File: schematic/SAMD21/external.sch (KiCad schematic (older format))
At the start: 19 parts, among them IC3 MCP2221-I_SL, J10 Conn_02x06_Odd_Even, J11 Conn_02x06_Odd_Even, J12 Conn_02x06_Odd_Even, J13 Conn_01x02, J14 Conn_02x05_Odd_Even, J15 Conn_01x08, J8 Conn_02x02_Odd_Even, J9 Conn_02x02_Odd_Even

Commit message: Complete schematic
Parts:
- J10: footprint (none) -> Connector_PinHeader_2.54mm:PinHeader_2x06_P2.54mm_Vertical
- J12: footprint (none) -> Connector_PinHeader_2.54mm:PinHeader_2x06_P2.54mm_Vertical_SMD
- J14: footprint (none) -> Connector_PinHeader_2.54mm:PinHeader_2x05_P2.54mm_Vertical
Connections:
- net labels added: D+, D-, PA02, PA03, PA04, PA05, PA06, PA07, PA08, PA09, PA10, PA11, PA12, PA13, PA14, PA15, PA16, PA17, PA18, PA19, PA20, PA21, PA22, PA23, PA27, PA28, PB08, PB09, PB10, PB11, PB22, PB23
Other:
- moved on the sheet: J11, J12, J14
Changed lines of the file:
@@
 L Connector_Generic:Conn_02x06_Odd_Even J11
 U 1 1 61799C22
-P 4850 5800
-F 0 "J11" H 4900 6125 50  0000 C CNN
-F 1 "Conn_02x06_Odd_Even" H 4900 6126 50  0001 C CNN
-F 2 "Connector_PinHeader_2.54mm:PinHeader_2x06_P2.54mm_Vertical" H 4850 5800 50  0001 C CNN
-F 3 "~" H 4850 5800 50  0001 C CNN
-	1    4850 5800
-	1    0    0    -1
-$EndComp
-Text GLabel 7200 4350 0    50   Input ~ 0
-VCC3V3
-Text GLabel 4550 5600 0    50   Input ~ 0
-VCC3V3
-Text GLabel 7500 5650 0    50   Input ~ 0
+P 4800 5800
+F 0 "J11" H 4850 6125 50  0000 C CNN
+F 1 "Conn_02x06_Odd_Even" H 4850 6126 50  0001 C CNN
+F 2 "Connector_PinHeader_2.54mm:PinHeader_2x06_P2.54mm_Vertical" H 4800 5800 50  0001 C CNN
+F 3 "~" H 4800 5800 50  0001 C CNN
+	1    4800 5800
+	1    0    0    -1
+$EndComp
+Text GLabel 7200 4300 0    50   Input ~ 0
+VCC3V3
+Text GLabel 4500 5600 0    50   Input ~ 0
+VCC3V3
+Text GLabel 7200 5600 0    50   Input ~ 0
 VCC3V3
 $Comp
 L power:GND #PWR029
 U 1 1 617AC5C9
-P 7800 4350
-F 0 "#PWR029" H 7800 4100 50  0001 C CNN
-F 1 "GND" V 7805 4222 50  0000 R CNN
-F 2 "" H 7800 4350 50  0001 C CNN
-F 3 "" H 7800 4350 50  0001 C CNN
-	1    7800 4350
+P 7800 4300
+F 0 "#PWR029" H 7800 4050 50  0001 C CNN
+F 1 "GND" V 7805 4172 50  0000 R CNN
+F 2 "" H 7800 4300 50  0001 C CNN
+F 3 "" H 7800 4300 50  0001 C CNN
+	1    7800 4300
 	0    -1   -1   0
 $EndComp
@@
 L power:GND #PWR027
 U 1 1 617B03D0
-P 5150 5600
-F 0 "#PWR027" H 5150 5350 50  0001 C CNN
-F 1 "GND" V 5155 5472 50  0000 R CNN
-F 2 "" H 5150 5600 50  0001 C CNN
-F 3 "" H 5150 5600 50  0001 C CNN
-	1    5150 5600
+P 5100 5600
+F 0 "#PWR027" H 5100 5350 50  0001 C CNN
+F 1 "GND" V 5105 5472 50  0000 R CNN
+F 2 "" H 5100 5600 50  0001 C CNN
+F 3 "" H 5100 5600 50  0001 C CNN
+	1    5100 5600
 	0    -1   -1   0
 $EndComp
@@
 L power:GND #PWR030
 U 1 1 617B4203
-P 8100 5650
-F 0 "#PWR030" H 8100 5400 50  0001 C CNN
-F 1 "GND" V 8105 5522 50  0000 R CNN
-F 2 "" H 8100 5650 50  0001 C CNN
-F 3 "" H 8100 5650 50  0001 C CNN
-	1    8100 5650
+P 7800 5600
+F 0 "#PWR030" H 7800 5350 50  0001 C CNN
+F 1 "GND" V 7805 5472 50  0000 R CNN
+F 2 "" H 7800 5600 50  0001 C CNN
+F 3 "" H 7800 5600 50  0001 C CNN
+	1    7800 5600
 	0    -1   -1   0
 $EndComp
@@
 	5200 4400 5100 4400
 Wire Wire Line
-	7200 4350 7300 4350
-Wire Wire Line
-	7300 4450 7200 4450
-Wire Wire Line
-	7200 4550 7300 4550
-Wire Wire Line
-	7300 4650 7200 4650
-Wire Wire Line
-	7200 4750 7300 4750
-Wire Wire Line
-	7300 4850 7200 4850
-Wire Wire Line
-	7900 4850 7800 4850
-Wire Wire Line
-	7800 4750 7900 4750
-Wire Wire Line
-	7900 4650 7800 4650
-Wire Wire Line
-	7800 4550 7900 4550
-Wire Wire Line
-	7900 4450 7800 4450
-Wire Wire Line
-	4550 5600 4650 5600
-Wire Wire Line
-	4650 5700 4550 5700
-Wire Wire Line
-	4550 5800 4650 5800
-Wire Wire Line
-	4650 5900 4550 5900
-Wire Wire Line
-	4550 6000 4650 6000
-Wire Wire Line
-	4550 6100 4650 6100
-Wire Wire Line
-	5150 6100 5250 6100
-Wire Wire Line
-	5250 6000 5150 6000
-Wire Wire Line
-	5150 5900 5250 5900
-Wire Wire Line
-	5250 5800 5150 5800
-Wire Wire Line
-	5150 5700 5250 5700
-Wire Wire Line
-	7600 5650 7500 5650
-Wire Wire Line
-	7500 5750 7600 5750
-Wire Wire Line
-	8100 5850 8200 5850
-Wire Wire Line
-	8200 5950 8100 5950
-Wire Wire Line
-	8100 6050 8200 6050
-Wire Wire Line
-	7600 6050 7500 6050
-Wire Wire Line
-	7500 5950 7600 5950
-Wire Wire Line
-	8100 5750 8200 5750
+	7200 4300 7300 4300
+Wire Wire Line
+	7300 4400 7200 4400
+Wire Wire Line
+	7200 4500 7300 4500
+Wire Wire Line
+	7300 4600 7200 4600
+Wire Wire Line
+	7200 4700 7300 4700
+Wire Wire Line
+	7300 4800 7200 4800
+Wire Wire Line
+	7900 4800 7800 4800
+Wire Wire Line
+	7800 4700 7900 4700
+Wire Wire Line
+	7900 4600 7800 4600
+Wire Wire Line
+	7800 4500 7900 4500
+Wire Wire Line
+	7900 4400 7800 4400
+Wire Wire Line
+	4500 5600 4600 5600
+Wire Wire Line
+	4600 5700 4500 5700
+Wire Wire Line
+	4500 5800 4600 5800
+Wire Wire Line
+	4600 5900 4500 5900
+Wire Wire Line
+	4500 6000 4600 6000
+Wire Wire Line
+	4500 6100 4600 6100
+Wire Wire Line
+	5100 6100 5200 6100
+Wire Wire Line
+	5200 6000 5100 6000
+Wire Wire Line
+	5100 5900 5200 5900
+Wire Wire Line
+	5200 5800 5100 5800
+Wire Wire Line
+	5100 5700 5200 5700
+Wire Wire Line
+	7300 5600 7200 5600
+Wire Wire Line
+	7200 5700 7300 5700
+Wire Wire Line
+	7800 5800 7900 5800
+Wire Wire Line
+	7900 5900 7800 5900
+Wire Wire Line
+	7800 6000 7900 6000
+Wire Wire Line
+	7300 6000 7200 6000
+Wire Wire Line
+	7200 5900 7300 5900
+Wire Wire Line
+	7800 5700 7900 5700
 $Comp
 L Connector_Generic:Conn_01x08 J15
@@
 Program/Debug
 Wire Wire Line
-	7500 5850 7600 5850
+	7200 5800 7300 5800
 Text Notes 2900 2900 0    50   ~ 0
 SERCOM1
@@
 F 0 "J10" H 4850 4825 50  0000 C CNN
 F 1 "Conn_02x06_Odd_Even" H 4850 4826 50  0001 C CNN
-F 2 "" H 4800 4500 50  0001 C CNN
+F 2 "Connector_PinHeader_2.54mm:PinHeader_2x06_P2.54mm_Vertical" H 4800 4500 50  0001 C CNN
 F 3 "~" H 4800 4500 50  0001 C CNN
 	1    4800 4500
@@
 L Connector_Generic:Conn_02x06_Odd_Even J12
 U 1 1 619CB274
-P 7500 4550
-F 0 "J12" H 7550 4875 50  0000 C CNN
-F 1 "Conn_02x06_Odd_Even" H 7550 4876 50  0001 C CNN
-F 2 "" H 7500 4550 50  0001 C CNN
-F 3 "~" H 7500 4550 50  0001 C CNN
-	1    7500 4550
+P 7500 4500
+F 0 "J12" H 7550 4825 50  0000 C CNN
+F 1 "Conn_02x06_Odd_Even" H 7550 4826 50  0001 C CNN
+F 2 "Connector_PinHeader_2.54mm:PinHeader_2x06_P2.54mm_Vertical_SMD" H 7500 4500 50  0001 C CNN
+F 3 "~" H 7500 4500 50  0001 C CNN
+	1    7500 4500
 	1    0    0    -1
 $EndComp
@@
 L Connector_Generic:Conn_02x05_Odd_Even J14
 U 1 1 619D2D7D
-P 7800 5850
-F 0 "J14" H 7850 6175 50  0000 C CNN
-F 1 "Conn_02x05_Odd_Even" H 7850 6176 50  0001 C CNN
-F 2 "" H 7800 5850 50  0001 C CNN
-F 3 "~" H 7800 5850 50  0001 C CNN
-	1    7800 5850
-	1    0    0    -1
-$EndComp
+P 7500 5800
+F 0 "J14" H 7550 6125 50  0000 C CNN
+F 1 "Conn_02x05_Odd_Even" H 7550 6126 50  0001 C CNN
+F 2 "Connector_PinHeader_2.54mm:PinHeader_2x05_P2.54mm_Vertical" H 7500 5800 50  0001 C CNN
+F 3 "~" H 7500 5800 50  0001 C CNN
+	1    7500 5800
+	1    0    0    -1
+$EndComp
+Text GLabel 4500 4400 0    50   Input ~ 0
+SERCOM1_PAD0
+Text GLabel 5200 4400 2    50   Input ~ 0
+SERCOM1_PAD1
+Text GLabel 4500 4500 0    50   Input ~ 0
+PA02
+Text GLabel 5200 4500 2    50   Input ~ 0
+PA03
+Text GLabel 4500 4600 0    50   Input ~ 0
+PB08
+Text GLabel 5200 4600 2    50   Input ~ 0
+PB09
+Text GLabel 4500 4700 0    50   Input ~ 0
+PA04
+Text GLabel 5200 4700 2    50   Input ~ 0
+PA05
+Text GLabel 4500 4800 0    50   Input ~ 0
+PA06
+Text GLabel 5200 4800 2    50   Input ~ 0
+PA07
+Text GLabel 4500 5700 0    50   Input ~ 0
+PA08
+Text GLabel 5200 5700 2    50   Input ~ 0
+PA09
+Text GLabel 4500 5800 0    50   Input ~ 0
+PA10
+Text GLabel 5200 5800 2    50   Input ~ 0
+PA11
+Text GLabel 4500 5900 0    50   Input ~ 0
+PB10
+Text GLabel 5200 5900 2    50   Input ~ 0
+PB11
+Text GLabel 4500 6000 0    50   Input ~ 0
+PA12
+Text GLabel 5200 6000 2    50   Input ~ 0
+PA13
+Text GLabel 4500 6100 0    50   Input ~ 0
+PA14
+Text GLabel 5200 6100 2    50   Input ~ 0
+PA15
+Text GLabel 7200 4400 0    50   Input ~ 0
+PA16
+Text GLabel 7900 4400 2    50   Input ~ 0
+PA17
+Text GLabel 7200 4500 0    50   Input ~ 0
+PA18
+Text GLabel 7900 4500 2    50   Input ~ 0
+PA19
+Text GLabel 7200 4600 0    50   Input ~ 0
+PA20
+Text GLabel 7900 4600 2    50   Input ~ 0
+PA21
+Text GLabel 7200 4700 0    50   Input ~ 0
+PA22
+Text GLabel 7900 4700 2    50   Input ~ 0
+PA23
+Text GLabel 7200 4800 0    50   Input ~ 0
+D-
+Text GLabel 7900 4800 2    50   Input ~ 0
+D+
+Text GLabel 7200 5700 0    50   Input ~ 0
+PB22
+Text GLabel 7900 5700 2    50   Input ~ 0
+PB23
+Text GLabel 7200 5800 0    50   Input ~ 0
+PA27
+Text GLabel 7900 5800 2    50   Input ~ 0
+PA28
+Text GLabel 7200 5900 0    50   Input ~ 0
+SWCLK
+Text GLabel 7900 5900 2    50   Input ~ 0
+SWDIO
+Text GLabel 7200 6000 0    50   Input ~ 0
+SERCOM5_PAD0
+Text GLabel 7900 6000 2    50   Input ~ 0
+SERCOM5_PAD1
 $EndSCHEMATC

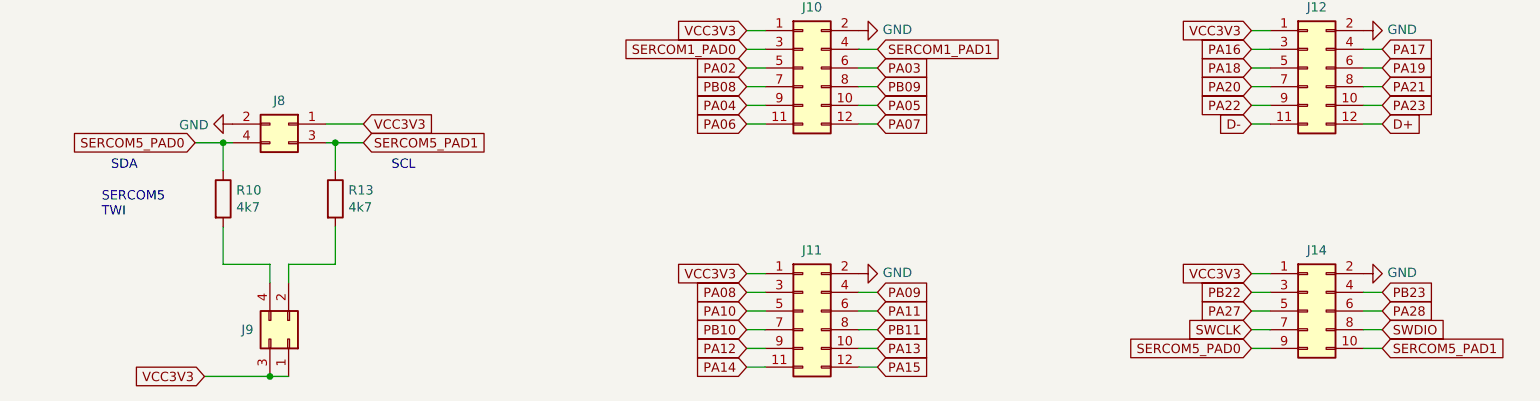
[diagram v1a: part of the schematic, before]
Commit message: Moved I2C to pins with support for I2C
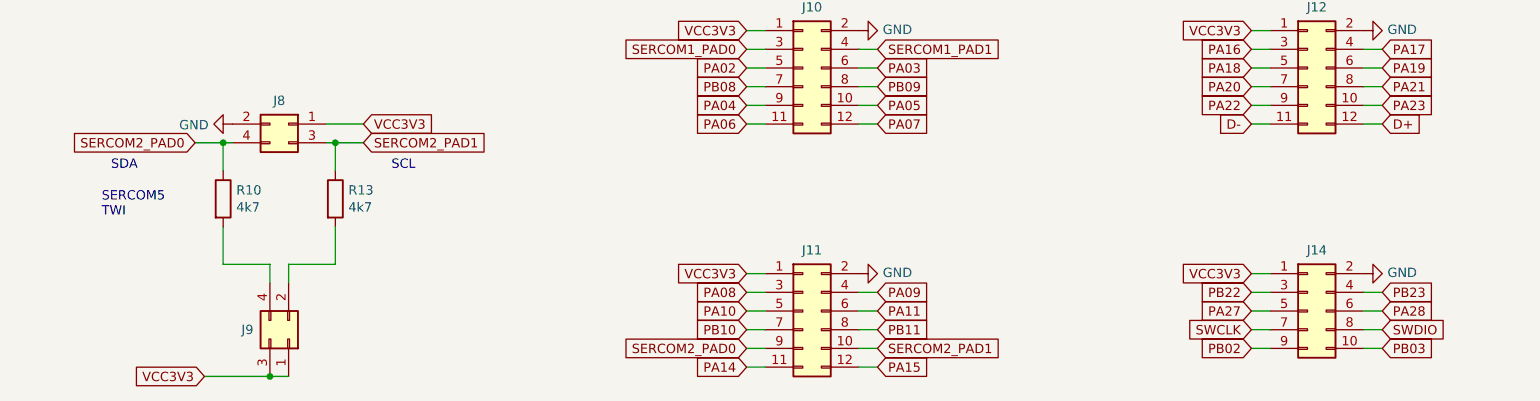
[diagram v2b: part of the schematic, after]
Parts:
- J12: footprint Connector_PinHeader_2.54mm:PinHeader_2x06_P2.54mm_Vertical_SMD -> Connector_PinHeader_2.54mm:PinHeader_2x06_P2.54mm_Vertical
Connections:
- net PA12 renamed SERCOM2_PAD0
- net SERCOM2_PAD0: now also J8.4 (Pin_4), R10.1
- net PA13 renamed SERCOM2_PAD1
- net SERCOM2_PAD1: now also J8.3 (Pin_3), R13.1
- removed net SERCOM5_PAD0: J14.9 (Pin_9), J8.4 (Pin_4), R10.1
- removed net SERCOM5_PAD1: J14.10 (Pin_10), J8.3 (Pin_3), R13.1
- new net PB02: J14.9 (Pin_9)
- new net PB03: J14.10 (Pin_10)
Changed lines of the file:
@@
 $EndComp
 Text GLabel 1550 4900 0    50   Input ~ 0
-SERCOM5_PAD0
+SERCOM2_PAD0
 Text GLabel 2450 4900 2    50   Input ~ 0
-SERCOM5_PAD1
+SERCOM2_PAD1
 Wire Wire Line
 	2250 4900 2300 4900
@@
 F 0 "J12" H 7550 4825 50  0000 C CNN
 F 1 "Conn_02x06_Odd_Even" H 7550 4826 50  0001 C CNN
-F 2 "Connector_PinHeader_2.54mm:PinHeader_2x06_P2.54mm_Vertical_SMD" H 7500 4500 50  0001 C CNN
+F 2 "Connector_PinHeader_2.54mm:PinHeader_2x06_P2.54mm_Vertical" H 7500 4500 50  0001 C CNN
 F 3 "~" H 7500 4500 50  0001 C CNN
 	1    7500 4500
@@
 PB11
 Text GLabel 4500 6000 0    50   Input ~ 0
-PA12
+SERCOM2_PAD0
 Text GLabel 5200 6000 2    50   Input ~ 0
-PA13
+SERCOM2_PAD1
 Text GLabel 4500 6100 0    50   Input ~ 0
 PA14
@@
 SWDIO
 Text GLabel 7200 6000 0    50   Input ~ 0
-SERCOM5_PAD0
+PB02
 Text GLabel 7900 6000 2    50   Input ~ 0
-SERCOM5_PAD1
+PB03
 $EndSCHEMATC
